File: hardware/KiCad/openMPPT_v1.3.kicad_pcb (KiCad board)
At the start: 2 copper layers, 70 x 80 mm, 135 parts, among them Q1 BSC030N08NS5, Q2 BSC030N08NS5, Q3 BSC030N08NS5, Q4 BSC030N08NS5, U1 STM32F072RBT6, U2 CC6937S8-3FB020, U3 CC6937S8-3FB020, U4 SCT2A25STER, U5 SY8120B1ABC

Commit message: fix: correct diode part data, select L4 inductor, drop DRC/ERC mandate
Diode inventory (D1-D7): replaced STANDARDS.md's fictional D_BOOT (US1M)
and D_OFF (1N4148W) rows - never actually placed - with the real,
schematic-verified parts: SS210 for both the gate-driver bootstrap role
(D1/D4) and gate-discharge role (D2/D3/D5/D6), and SS510 as the SCT2A25
switch-node freewheeling diode (D7). Fixes the PCB footprint mismatch on
D2/D3/D5/D6 (D_SOD-123 -> D_SMA, matching what the schematic already
specified and SS210 actually needs) and the JLCPCB/PCM_JLCPCB library
nickname mismatch on UA1/UB1's footprint reference.

L4 main inductor: replaced FC-SE2822-150M with HCZH-3218-150-M (C53699952)
in the schematic - same 15uH, lower DCR (3.5mOhm -> 2.2mOhm, cutting
conduction loss from 1.40W to 0.88W) for a $1.56 premium. Chosen after
evaluating and rejecting a higher-margin option (RSEQ32-220M) that cost
2.7x more and had far less stock for headroom this design doesn't need.
Full reasoning and rejected alternatives documented in CALCULATIONS.typ
Section 8. PCB footprint not yet updated for L4 (different pad format,
needs a deliberate swap, not a drop-in edit).

DRC/ERC: removed the "Claude runs kicad-cli DRC/ERC" mandate from
STANDARDS.md - board correctness review is the user's job, not something
to check automatically or by default.

Co-Authored-By: Claude Sonnet 5 <noreply@anthropic.com>
Claude-Session: https://claude.ai/code/session_01FKwww6crXDCSrRUFRETJEs
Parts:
- L4: value FC-SE2822-150M -> HCZH-3218-150-M; footprint easyeda2kicad:IND-TH_L28.0-W23.0_FC-SE2822 -> easyeda2kicad:IND-TH_L33.5-W23.0-P12.00_HCZH-3218
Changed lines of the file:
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@@
 		)
 	)
-	(footprint "easyeda2kicad:IND-TH_L28.0-W23.0_FC-SE2822"
+	(footprint "easyeda2kicad:IND-TH_L33.5-W23.0-P12.00_HCZH-3218"
 		(layer "F.Cu")
 		(at 86.173 62.762)
@@
 			)
 		)
-		(property "Value" "FC-SE2822-150M"
+		(property "Value" "HCZH-3218-150-M"
 			(at 0 13.125 0)
 			(layer "F.Fab")
@@
 			)
 		)
-		(property "Datasheet" "https://www.lcsc.com/datasheet/C46553544.pdf"
+		(property "Datasheet" "https://www.lcsc.com/datasheet/C53699952.pdf"
 			(at 0 0 0)
 			(layer "F.Fab")
@@
 			)
 		)
-		(property "LCSC Part" "C46553544"
+		(property "LCSC Part" "C53699952"
 			(at 0 0 0)
 			(layer "F.Fab")
@@
 			)
 		)
-		(property "Manufacturer" "FC(方成)"
+		(property "Manufacturer" "YOUCHI(佑驰)"
 			(at 0 0 0)
 			(unlocked yes)
@@
 			)
 		)
-		(property "MPN" "FC-SE2822-150M"
+		(property "MPN" "HCZH-3218-150-M"
 			(at 0 0 0)
 			(unlocked yes)
@@
 		(duplicate_pad_numbers_are_jumpers no)
 		(fp_line
-			(start -14.5 -10)
-			(end -14.5 10)
-			(stroke
-				(width 0.25)
-				(type solid)
-			)
-			(layer "F.SilkS")
-		)
-		(fp_line
-			(start -5 -12)
-			(end -5 -10)
-			(stroke
-				(width 0.25)
-				(type solid)
-			)
-			(layer "F.SilkS")
-		)
-		(fp_line
-			(start -5 -12)
-			(end 5 -12)
-			(stroke
-				(width 0.25)
-				(type solid)
-			)
-			(layer "F.SilkS")
-		)
-		(fp_line
-			(start -5 -10)
-			(end -14.5 -10)
-			(stroke
-				(width 0.25)
-				(type solid)
-			)
-			(layer "F.SilkS")
-		)
-		(fp_line
-			(start -5 10)
-			(end -14.5 10)
-			(stroke
-				(width 0.25)
-				(type solid)
-			)
-			(layer "F.SilkS")
-		)
-		(fp_line
-			(start -5 12)
-			(end -5 10)
-			(stroke
-				(width 0.25)
-				(type solid)
-			)
-			(layer "F.SilkS")
-		)
-		(fp_line
-			(start 5 -12)
-			(end 5 -10)
-			(stroke
-				(width 0.25)
-				(type solid)
-			)
-			(layer "F.SilkS")
-		)
-		(fp_line
-			(start 5 -10)
-			(end 14.5 -10)
-			(stroke
-				(width 0.25)
-				(type solid)
-			)
-			(layer "F.SilkS")
-		)
-		(fp_line
-			(start 5 10)
-			(end 14.5 10)
-			(stroke
-				(width 0.25)
-				(type solid)
-			)
-			(layer "F.SilkS")
-		)
-		(fp_line
-			(start 5 12)
-			(end -5 12)
-			(stroke
-				(width 0.25)
-				(type solid)
-			)
-			(layer "F.SilkS")
-		)
-		(fp_line
-			(start 5 12)
-			(end 5 10)
-			(stroke
-				(width 0.25)
-				(type solid)
-			)
-			(layer "F.SilkS")
-		)
-		(fp_line
-			(start 14.5 -10)
-			(end 14.5 10)
+			(start 9.02 -3.43)
+			(end 9.02 -1.65)
+			(stroke
+				(width 0.25)
+				(type solid)
+			)
+			(layer "F.SilkS")
+		)
+		(fp_line
+			(start 3.01 -3.43)
+			(end 3.01 -1.78)
+			(stroke
+				(width 0.25)
+				(type solid)
+			)
+			(layer "F.SilkS")
+		)
+		(fp_line
+			(start 3.01 -2.07)
+			(end 3.01 -1.66)
+			(stroke
+				(width 0.25)
+				(type solid)
+			)
+			(layer "F.SilkS")
+		)
+		(fp_line
+			(start -8.99 -2.07)
+			(end -8.99 -1.66)
+			(stroke
+				(width 0.25)
+				(type solid)
+			)
+			(layer "F.SilkS")
+		)
+		(fp_line
+			(start -2.98 -3.43)
+			(end -2.98 -1.65)
+			(stroke
+				(width 0.25)
+				(type solid)
+			)
+			(layer "F.SilkS")
+		)
+		(fp_line
+			(start -8.99 -3.43)
+			(end -8.99 -1.78)
+			(stroke
+				(width 0.25)
+				(type solid)
+			)
+			(layer "F.SilkS")
+		)
+		(fp_line
+			(start -16.76 -3.43)
+			(end -16.76 -26.54)
+			(stroke
+				(width 0.25)
+				(type solid)
+			)
+			(layer "F.SilkS")
+		)
+		(fp_line
+			(start -16.76 -26.54)
+			(end 16.76 -26.54)
+			(stroke
+				(width 0.25)
+				(type solid)
+			)
+			(layer "F.SilkS")
+		)
+		(fp_line
+			(start 16.76 -26.54)
+			(end 16.76 -3.43)
+			(stroke
+				(width 0.25)
+				(type solid)
+			)
+			(layer "F.SilkS")
+		)
+		(fp_line
+			(start 16.76 -3.43)
+			(end -16.76 -3.43)
 			(stroke
 				(width 0.25)
@@
 		)
 		(fp_circle
-			(center -14.5 -12)
-			(end -14.47 -12)
+			(center -16.75 0.50)
+			(end -16.72 0.50)
 			(stroke
 				(width 0.06)
@@
 		)
 		(fp_line
-			(start -14.5 -10)
-			(end -14.5 10)
-			(stroke
-				(width 0.05)
-				(type solid)
-			)
-			(layer "F.CrtYd")
-		)
-		(fp_line
-			(start -14.5 10)
-			(end -5 10)
-			(stroke
-				(width 0.05)
-				(type solid)
-			)
-			(layer "F.CrtYd")
-		)
-		(fp_line
-			(start -5 -12)
-			(end -5 -10)
-			(stroke
-				(width 0.05)
-				(type solid)
-			)
-			(layer "F.CrtYd")
-		)
-		(fp_line
-			(start -5 -10)
-			(end -14.5 -10)
-			(stroke
-				(width 0.05)
-				(type solid)
-			)
-			(layer "F.CrtYd")
-		)
-		(fp_line
-			(start -5 10)
-			(end -5 12)
-			(stroke
-				(width 0.05)
-				(type solid)
-			)
-			(layer "F.CrtYd")
-		)
-		(fp_line
-			(start -5 12)
-			(end 5 12)
-			(stroke
-				(width 0.05)
-				(type solid)
-			)
-			(layer "F.CrtYd")
-		)
-		(fp_line
-			(start 5 -12)
-			(end -5 -12)
-			(stroke
-				(width 0.05)
-				(type solid)
-			)
-			(layer "F.CrtYd")
-		)
-		(fp_line
-			(start 5 -10)
-			(end 5 -12)
-			(stroke
-				(width 0.05)
-				(type solid)
-			)
-			(layer "F.CrtYd")
-		)
-		(fp_line
-			(start 5 10)
-			(end 14.5 10)
-			(stroke
-				(width 0.05)
-				(type solid)
-			)
-			(layer "F.CrtYd")
-		)
-		(fp_line
-			(start 5 12)
-			(end 5 10)
-			(stroke
-				(width 0.05)
-				(type solid)
-			)
-			(layer "F.CrtYd")
-		)
-		(fp_line
-			(start 14.5 -10)
-			(end 5 -10)
-			(stroke
-				(width 0.05)
-				(type solid)
-			)
-			(layer "F.CrtYd")
-		)
-		(fp_line
-			(start 14.5 10)
-			(end 14.5 -10)
-			(stroke
-				(width 0.05)
-				(type solid)
-			)
-			(layer "F.CrtYd")
-		)
-		(fp_circle
-			(center 0 -9.13)
-			(end 0.58 -9.13)
-			(stroke
-				(width 1.15)
-				(type solid)
-			)
-			(fill no)
-			(layer "F.Fab")
-		)
-		(fp_circle
-			(center 0 9.12)
-			(end 0.58 9.12)
-			(stroke
-				(width 1.15)
-				(type solid)
-			)
-			(fill no)
-			(layer "F.Fab")
-		)
-		(fp_text user "${REFERENCE}"
-			(at 0 0 0)
-			(layer "F.Fab")
-			(effects
-				(font
-					(size 1 1)
-					(thickness 0.15)
-				)
-			)
-		)
-		(pad "1" thru_hole circle
-			(at 0 -9.13)
-			(size 3.7 3.7)
-			(drill 2.50002)
+			(start -16.75 -3.5)
+			(end -16.75 -26.5)
+			(stroke
+				(width 0.05)
+				(type solid)
+			)
+			(layer "F.CrtYd")
+		)
+		(fp_line
+			(start -16.75 -26.5)
+			(end 16.75 -26.5)
+			(stroke
+				(width 0.05)
+				(type solid)
+			)
+			(layer "F.CrtYd")
+		)
+		(fp_line
+			(start 16.75 -26.5)
+			(end 16.75 -3.5)
+			(stroke
+				(width 0.05)
+				(type solid)
+			)
+			(layer "F.CrtYd")
+		)
+		(fp_line
+			(start 16.75 -3.5)
+			(end -16.75 -3.5)
+			(stroke
+				(width 0.05)
+				(type solid)
+			)
+			(layer "F.CrtYd")
+		)
+		(pad "1" thru_hole oval
+			(at -6.00 0.00)
+			(size 8.000 3.000)
+			(drill oval 6.599987 1.599996)
 			(layers "*.Cu" "*.Mask")
-			(remove_unused_layers no)
 			(net "VS_A")
-			(pinfunction "1_1")
 			(pintype "unspecified")
 		)
-		(pad "2" thru_hole circle
-			(at 0 9.12)
-			(size 3.7 3.7)
-			(drill 2.50002)
+		(pad "2" thru_hole oval
+			(at 6.00 0.00)
+			(size 8.000 3.000)
+			(drill oval 6.599987 1.599996)
 			(layers "*.Cu" "*.Mask")
-			(remove_unused_layers no)
 			(net "VS_B")
-			(pinfunction "2_2")
 			(pintype "unspecified")
 		)
 		(embedded_fonts no)
-		(model "${EASYEDA2KICAD}/easyeda2kicad.3dshapes/IND-TH_L28.0-W23.0_FC-SE2822.wrl"
+		(model "${KIPRJMOD}/hardware/KiCad/libraries/easyeda2kicad/easyeda2kicad.3dshapes/IND-TH_L33.5-W23.0-P12.00_HCZH-3218.wrl"
 			(offset
 				(xyz 0 0 0)

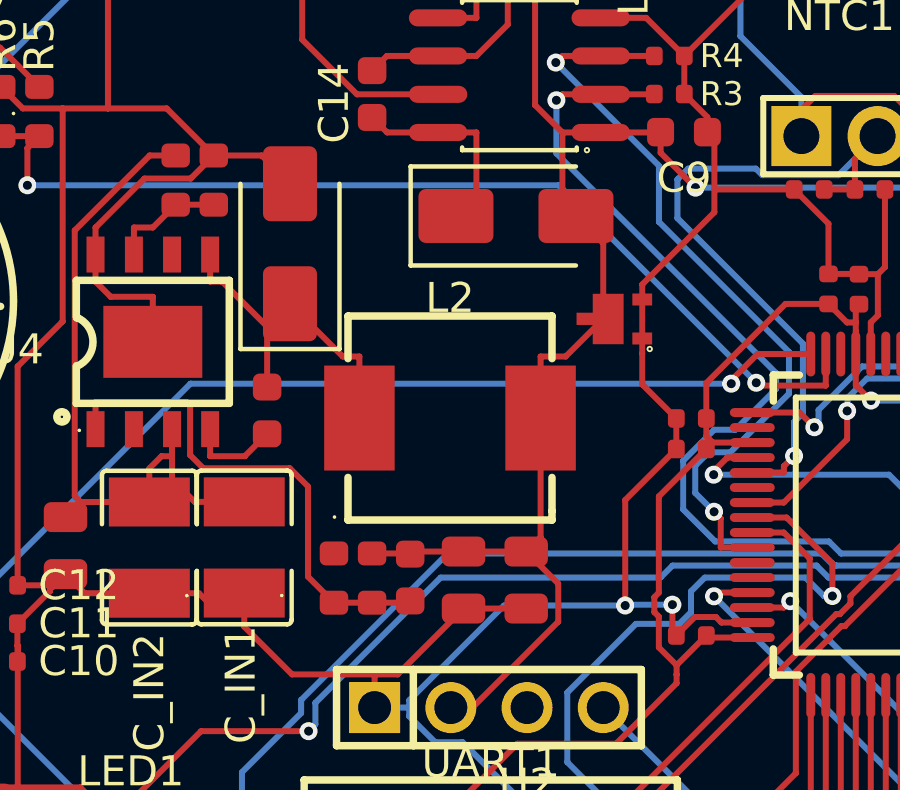
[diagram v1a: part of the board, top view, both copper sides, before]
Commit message: fix: upsize L2 aux inductor for fault-current headroom
Replaces APS0650M470A (47uH, Isat 2.62A, DCR 227mOhm) with GXDR1207-470MT
(FAUKU, C52196367, $0.207, 11735 in stock) for L2, the SCT2A25 10V rail's
inductor. Same 47uH, but Isat now matches SCT2A25's own 4A peak current
limit exactly instead of saturating well below it, and DCR drops to
90mOhm. The original part was sized for the baseline gate-driver/logic
load (~150-500mA), not for a heavier load (e.g. a fan) that might get
added to the 10V rail - same underlying reasoning as why D7 stays SS510
instead of SS210. Applied to both the schematic and PCB (package grew
from 7.7x6.6mm to 12.5x12.5mm SMD).

Co-Authored-By: Claude Sonnet 5 <noreply@anthropic.com>
Claude-Session: https://claude.ai/code/session_01FKwww6crXDCSrRUFRETJEs
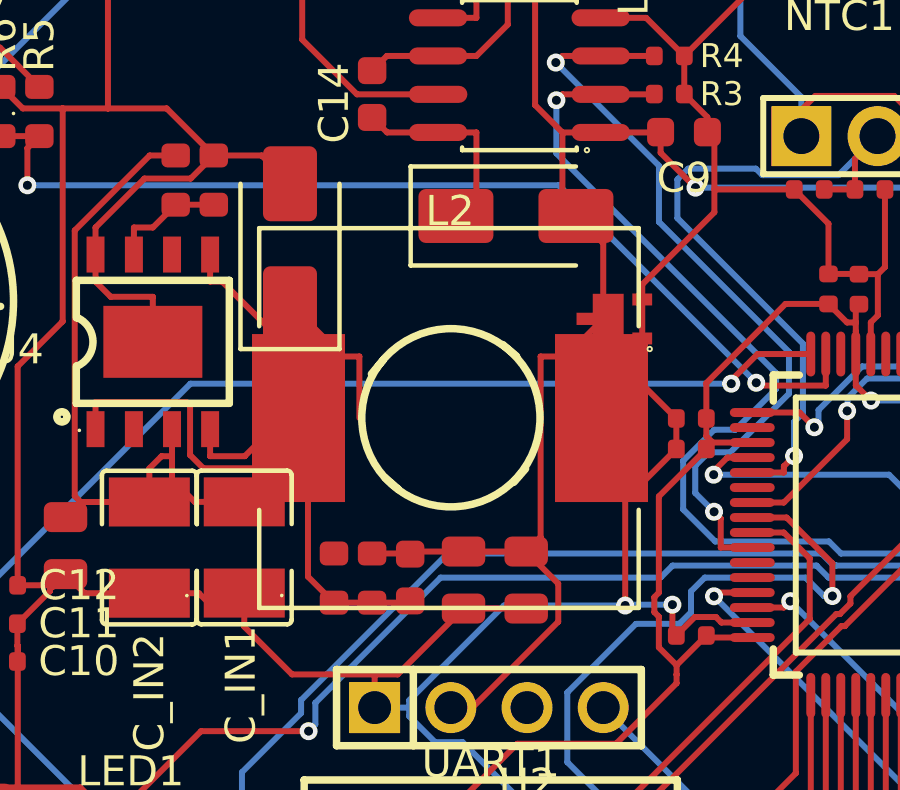
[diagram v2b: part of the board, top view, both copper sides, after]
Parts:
- L2: footprint easyeda2kicad:IND-SMD_L7.7-W6.6_APS07A30M220 -> easyeda2kicad:IND-SMD_L12.5-W12.5-1
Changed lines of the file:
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@@
 		)
 	)
-	(footprint "easyeda2kicad:IND-SMD_L7.7-W6.6_APS07A30M220"
+	(footprint "easyeda2kicad:IND-SMD_L12.5-W12.5-1"
 		(layer "F.Cu")
 		(at 77.95 98.806)
 		(property "Reference" "L2"
-			(at 0 -4 0)
+			(at 0 -6.9 0)
 			(layer "F.SilkS")
 			(effects
@@
 		)
 		(property "Value" "47uH"
-			(at 0 4 0)
-			(layer "F.Fab")
-			(effects
-				(font
-					(size 1 1)
-					(thickness 0.15)
-				)
-			)
-		)
-		(property "Datasheet" "https://www.lcsc.com/datasheet/C47327224.pdf"
+			(at 0 6.9 0)
+			(layer "F.Fab")
+			(effects
+				(font
+					(size 1 1)
+					(thickness 0.15)
+				)
+			)
+		)
+		(property "Datasheet" "https://www.lcsc.com/datasheet/C52196367.pdf"
 			(at 0 0 0)
 			(layer "F.Fab")
@@
 			)
 		)
-		(property "LCSC Part" "C47327224"
+		(property "LCSC Part" "C52196367"
 			(at 0 0 0)
 			(layer "F.Fab")
@@
 			)
 		)
-		(property "Manufacturer" "Coilank(驰兴电感)"
+		(property "Manufacturer" "FAUKU(高芯电子)"
 			(at 0 0 0)
 			(unlocked yes)
@@
 			)
 		)
-		(property "MPN" "APS0650M470A"
+		(property "MPN" "GXDR1207-470MT"
 			(at 0 0 0)
 			(unlocked yes)
@@
 			)
 		)
-		(attr through_hole)
+		(attr smd)
 		(duplicate_pad_numbers_are_jumpers no)
 		(fp_line
-			(start -3.4 -3.4)
-			(end -3.4 -1.98)
-			(stroke
-				(width 0.25)
-				(type solid)
-			)
-			(layer "F.SilkS")
-		)
-		(fp_line
-			(start -3.4 -3.4)
-			(end 3.4 -3.4)
-			(stroke
-				(width 0.25)
-				(type solid)
-			)
-			(layer "F.SilkS")
-		)
-		(fp_line
-			(start -3.4 1.98)
-			(end -3.4 3.4)
-			(stroke
-				(width 0.25)
-				(type solid)
-			)
-			(layer "F.SilkS")
-		)
-		(fp_line
-			(start 3.4 -1.98)
-			(end 3.4 -3.4)
-			(stroke
-				(width 0.25)
-				(type solid)
-			)
-			(layer "F.SilkS")
-		)
-		(fp_line
-			(start 3.4 3.1)
-			(end 3.4 1.98)
-			(stroke
-				(width 0.25)
-				(type solid)
-			)
-			(layer "F.SilkS")
-		)
-		(fp_line
-			(start 3.4 3.1)
-			(end 3.4 3.4)
-			(stroke
-				(width 0.25)
-				(type solid)
-			)
-			(layer "F.SilkS")
-		)
-		(fp_line
-			(start 3.4 3.4)
-			(end -3.4 3.4)
+			(start -6.36 -3.06)
+			(end -6.36 -6.33)
+			(stroke
+				(width 0.15)
+				(type solid)
+			)
+			(layer "F.SilkS")
+		)
+		(fp_line
+			(start -6.36 -6.33)
+			(end 6.29 -6.33)
+			(stroke
+				(width 0.15)
+				(type solid)
+			)
+			(layer "F.SilkS")
+		)
+		(fp_line
+			(start 6.29 -6.33)
+			(end 6.29 -3.06)
+			(stroke
+				(width 0.15)
+				(type solid)
+			)
+			(layer "F.SilkS")
+		)
+		(fp_line
+			(start -6.36 3.06)
+			(end -6.36 6.33)
+			(stroke
+				(width 0.15)
+				(type solid)
+			)
+			(layer "F.SilkS")
+		)
+		(fp_line
+			(start -6.36 6.33)
+			(end 6.29 6.33)
+			(stroke
+				(width 0.15)
+				(type solid)
+			)
+			(layer "F.SilkS")
+		)
+		(fp_line
+			(start 6.29 6.33)
+			(end 6.29 3.06)
+			(stroke
+				(width 0.15)
+				(type solid)
+			)
+			(layer "F.SilkS")
+		)
+		(fp_line
+			(start -2.23 -1.93)
+			(end -2.62 -1.47)
+			(stroke
+				(width 0.25)
+				(type solid)
+			)
+			(layer "F.SilkS")
+		)
+		(fp_line
+			(start 2.22 -2.06)
+			(end 1.76 -2.45)
+			(stroke
+				(width 0.25)
+				(type solid)
+			)
+			(layer "F.SilkS")
+		)
+		(fp_line
+			(start -2.17 1.98)
+			(end -1.72 2.37)
+			(stroke
+				(width 0.25)
+				(type solid)
+			)
+			(layer "F.SilkS")
+		)
+		(fp_line
+			(start 2.13 2.14)
+			(end 2.52 1.69)
 			(stroke
 				(width 0.25)
@@
 		)
 		(fp_circle
-			(center -3.85 3.3)
-			(end -3.82 3.3)
+			(center 6.25 -6.25)
+			(end 6.28 -6.25)
 			(stroke
 				(width 0.06)
@@
 			(layer "F.SilkS")
 		)
-		(fp_line
-			(start -3.3 -3.3)
-			(end 3.3 -3.3)
-			(stroke
-				(width 0.05)
-				(type solid)
-			)
-			(layer "F.CrtYd")
-		)
-		(fp_line
-			(start -3.3 3.3)
-			(end -3.3 -3.3)
-			(stroke
-				(width 0.05)
-				(type solid)
-			)
-			(layer "F.CrtYd")
-		)
-		(fp_line
-			(start 3.3 -3.3)
-			(end 3.3 3.3)
-			(stroke
-				(width 0.05)
-				(type solid)
-			)
-			(layer "F.CrtYd")
-		)
-		(fp_line
-			(start 3.3 3.3)
-			(end -3.3 3.3)
-			(stroke
-				(width 0.05)
-				(type solid)
-			)
-			(layer "F.CrtYd")
-		)
-		(fp_text user "${REFERENCE}"
-			(at 0 0 0)
-			(layer "F.Fab")
-			(effects
-				(font
-					(size 1 1)
-					(thickness 0.15)
-				)
-			)
+		(fp_circle
+			(center 0.03 -0.01)
+			(end 3.00 -0.01)
+			(stroke
+				(width 0.25)
+				(type solid)
+			)
+			(fill no)
+			(layer "F.SilkS")
+		)
+		(fp_line
+			(start -6.25 6.25)
+			(end -6.25 -6.25)
+			(stroke
+				(width 0.05)
+				(type solid)
+			)
+			(layer "F.CrtYd")
+		)
+		(fp_line
+			(start -6.25 -6.25)
+			(end 6.25 -6.25)
+			(stroke
+				(width 0.05)
+				(type solid)
+			)
+			(layer "F.CrtYd")
+		)
+		(fp_line
+			(start 6.25 -6.25)
+			(end 6.25 6.25)
+			(stroke
+				(width 0.05)
+				(type solid)
+			)
+			(layer "F.CrtYd")
+		)
+		(fp_line
+			(start 6.25 6.25)
+			(end -6.25 6.25)
+			(stroke
+				(width 0.05)
+				(type solid)
+			)
+			(layer "F.CrtYd")
 		)
 		(pad "1" smd rect
-			(at -3.02 0 270)
-			(size 3.5 2.35)
-			(layers "F.Cu" "F.Mask" "F.Paste")
+			(at 5.05 0.00)
+			(size 3.100 5.600)
+			(layers "F.Cu" "F.Paste" "F.Mask")
 			(net "Net-(U4-SW)")
-			(pinfunction "1_1")
 			(pintype "unspecified")
 		)
 		(pad "2" smd rect
-			(at 3.02 0 270)
-			(size 3.5 2.35)
-			(layers "F.Cu" "F.Mask" "F.Paste")
+			(at -5.05 0.00)
+			(size 3.100 5.600)
+			(layers "F.Cu" "F.Paste" "F.Mask")
 			(net "+10V")
-			(pinfunction "2_2")
 			(pintype "unspecified")
 		)
 		(embedded_fonts no)
-		(model "${EASYEDA2KICAD}/easyeda2kicad.3dshapes/IND-SMD_L7.7-W6.6-H3.0_APS07A30M220.wrl"
+		(model "${KIPRJMOD}/hardware/KiCad/libraries/easyeda2kicad/easyeda2kicad.3dshapes/IND-SMD_L12.5-W12.5-1.wrl"
 			(offset
 				(xyz 0 0 0)
@@
 			)
 			(rotate
-				(xyz 0 0 0)
-			)
-		)
+				(xyz 0 0 270)
+			)
+		)
